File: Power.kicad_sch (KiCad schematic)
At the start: 82 parts, among them J11 8-pin ATX connector, Q1 MMBT2222A, U21 SiRA80DP, U22 TPS25983, U23 AP7361C-33ER, U24 MP8795, U25 MIC23201YML-TR

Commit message: Corrected calculations of MP8795's external components
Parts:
- L2: value 4.7nH -> 4.7uH; footprint Inductor_SMD:L_6.3x6.3_H3 -> Inductor_SMD:L_Coilcraft_XAL1010-XXX; LCSC Part (none) -> C19271849; Mouser Part No  (none) -> 710-7843250072
- L3: value 1.5u -> 1.5uH
- R81: value 8.2k -> 8k; footprint Resistor_SMD:R_0402_1005Metric -> Resistor_SMD:R_0603_1608Metric; LCSC Part C137929 -> C862307
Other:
- note added: "for current ripple 0.00075A"
- note removed: "for current ripple 0.75A"
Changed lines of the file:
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@@
 		)
 	)
-	(text "for current ripple 0.75A"
+	(text "for current ripple 0.00075A"
 		(exclude_from_sim no)
-		(at 134.112 92.456 0)
+		(at 143.51 92.456 0)
 		(effects
 			(font
@@
 			)
 		)
-		(property "Value" "1.5u"
+		(property "Value" "1.5uH"
 			(at 109.22 162.56 90)
 			(effects
@@
 			)
 		)
-		(property "Value" "8.2k"
+		(property "Value" "8k"
 			(at 62.23 120.6499 0)
 			(effects
@@
 			)
 		)
-		(property "Footprint" "Resistor_SMD:R_0402_1005Metric"
+		(property "Footprint" "Resistor_SMD:R_0603_1608Metric"
 			(at 57.912 119.38 90)
 			(effects
@@
 			)
 		)
-		(property "LCSC Part" "C137929"
+		(property "LCSC Part" "C862307"
 			(at 59.69 119.38 0)
 			(effects
@@
 			)
 		)
-		(property "Value" "4.7nH"
+		(property "Value" "4.7uH"
 			(at 118.11 92.202 90)
 			(effects
@@
 			)
 		)
-		(property "Footprint" "Inductor_SMD:L_6.3x6.3_H3"
+		(property "Footprint" "Inductor_SMD:L_Coilcraft_XAL1010-XXX"
 			(at 118.11 93.98 0)
 			(effects
@@
 			(effects
 				(font
+					(size 1.27 1.27)
+				)
+				(hide yes)
+			)
+		)
+		(property "Mouser Part No " "710-7843250072 "
+			(at 118.11 93.98 90)
+			(effects
+				(font
+					(size 1.27 1.27)
+				)
+				(hide yes)
+			)
+		)
+		(property "LCSC Part" "C19271849"
+			(at 118.11 93.98 90)
+			(effects
+				(font

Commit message: minor schematic fixes, footprints changes, layout improvements
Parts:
- C114, C117: footprint Capacitor_THT:C_Radial_D5.0mm_H11.0mm_P2.00mm -> Capacitor_SMD:C_1812_4532Metric; LCSC Part C88755 -> C141660
- L3: LCSC Part (none) -> C520330
- TP7, TP8: footprint TestPoint:TestPoint_Loop_D1.80mm_Drill1.0mm_Beaded -> TestPoint:TestPoint_Pad_D1.0mm
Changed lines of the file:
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@@
 			)
 		)
-		(property "Footprint" "TestPoint:TestPoint_Loop_D1.80mm_Drill1.0mm_Beaded"
+		(property "Footprint" "TestPoint:TestPoint_Pad_D1.0mm"
 			(at 128.27 165.1 0)
 			(effects
@@
 			)
 		)
-		(property "Footprint" "TestPoint:TestPoint_Loop_D1.80mm_Drill1.0mm_Beaded"
+		(property "Footprint" "TestPoint:TestPoint_Pad_D1.0mm"
 			(at 274.32 93.98 0)
 			(effects
@@
 			)
 		)
-		(property "Footprint" "Capacitor_THT:C_Radial_D5.0mm_H11.0mm_P2.00mm"
+		(property "Footprint" "Capacitor_SMD:C_1812_4532Metric"
 			(at 134.3152 172.72 0)
 			(effects
@@
 			)
 		)
-		(property "LCSC Part" "C88755"
+		(property "LCSC Part" "C141660 "
 			(at 133.35 168.91 0)
 			(effects
@@
 			)
 		)
+		(property "LCSC Part" "C520330"
+			(at 109.22 165.1 90)
+			(effects
+				(font
+					(size 1.27 1.27)
+				)
+				(hide yes)
+			)
+		)
 		(pin "1"
 		)
@@
 			)
 		)
-		(property "Footprint" "Capacitor_THT:C_Radial_D5.0mm_H11.0mm_P2.00mm"
+		(property "Footprint" "Capacitor_SMD:C_1812_4532Metric"
 			(at 23.8252 172.72 0)
 			(effects
@@
 			)
 		)
-		(property "LCSC Part" "C88755"
+		(property "LCSC Part" "C141660 "
 			(at 22.86 168.91 0)
 			(effects

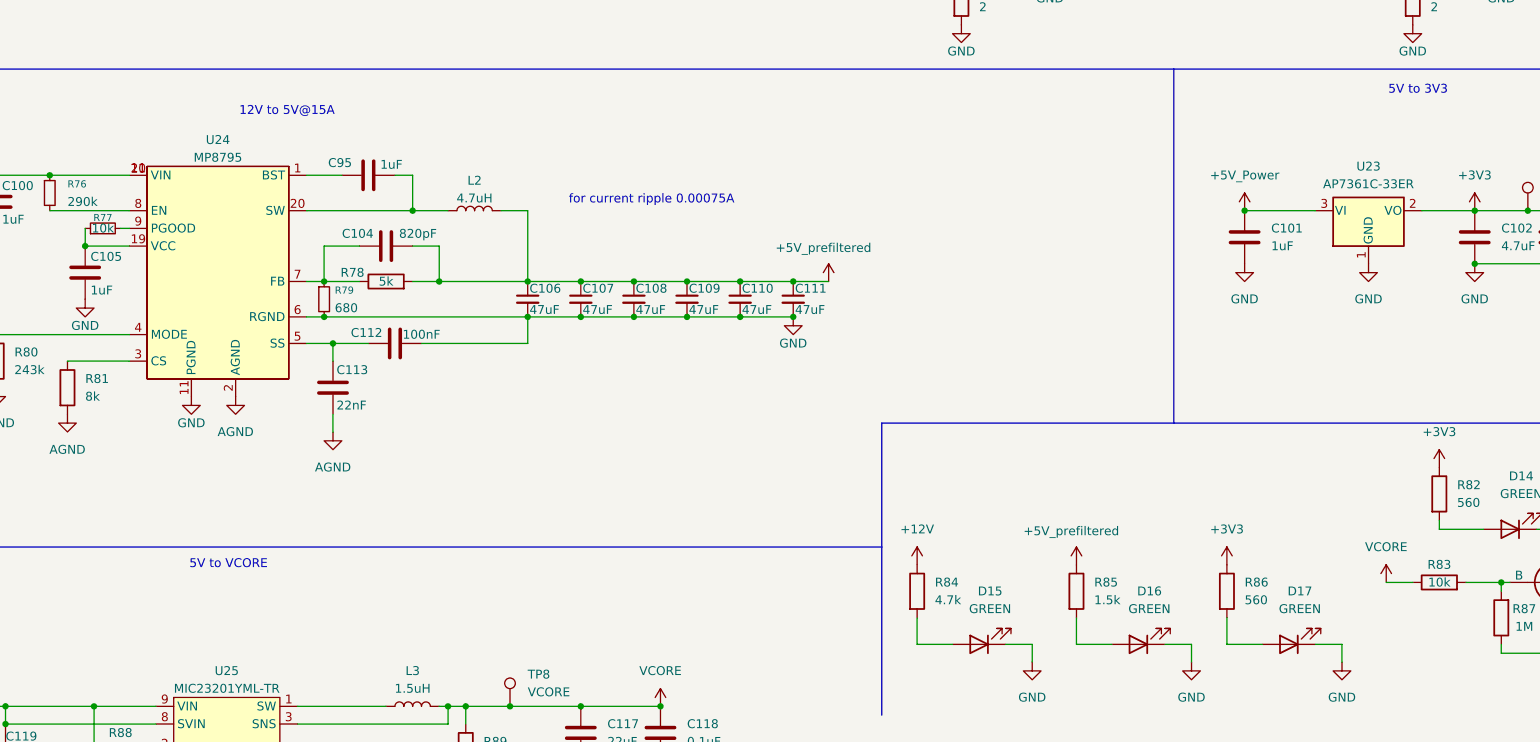
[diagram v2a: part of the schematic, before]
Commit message: comments to schematic added, changed a few components
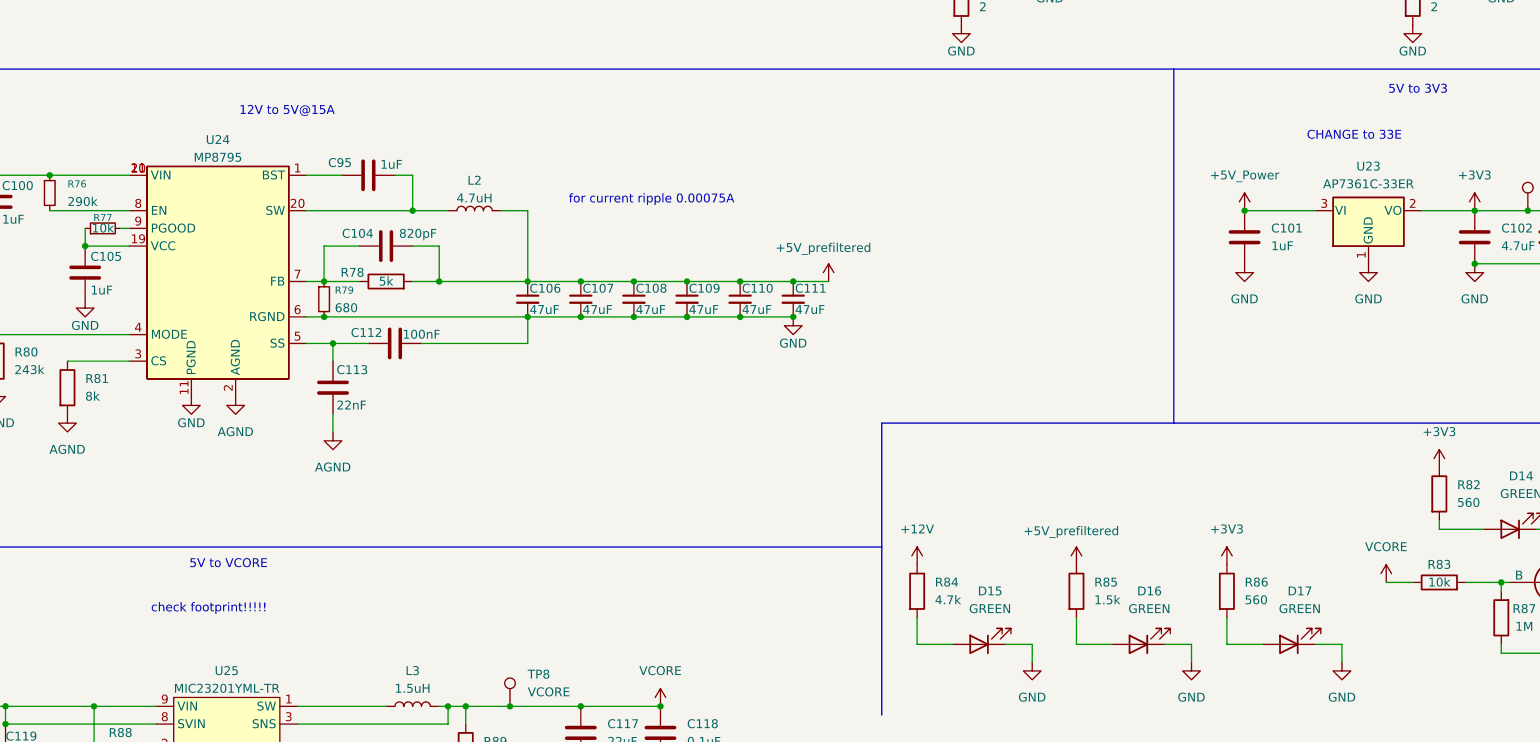
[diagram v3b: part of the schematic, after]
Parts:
- FB1, FB2, FB3: Mouser Part No  (none) -> 710-7427934
- J11: Mouser Part No  (none) -> 538-45586-0005; Mouser Part Number 538-45586-0005 -> (none)
- L2: LCSC Part C19271849 -> C18199458; Mouser Part No  710-7843250072 -> (none)
- U21: Mouser Part No  (none) -> 78-SIRA80DP-T1-RE3
- U22: LCSC Part (none) -> C20611808
- U23: LCSC Part C3743528 -> C500795
- U24: LCSC Part (none) -> C3188708
- U25: Mouser Part No  (none) -> 998-MIC23201YMLTR
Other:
- note added: "CHANGE to 33E"
- note added: "check footprint!!!!!"
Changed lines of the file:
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@@
 		)
 	)
+	(text "check footprint!!!!!"
+		(exclude_from_sim no)
+		(at 80.01 151.13 0)
+		(effects
+			(font
+				(size 1.27 1.27)
+			)
+		)
+	)
+	(text "CHANGE to 33E\n"
+		(exclude_from_sim no)
+		(at 244.348 83.312 0)
+		(effects
+			(font
+				(size 1.27 1.27)
+			)
+		)
+	)
 	(text "for current ripple 0.00075A"
 		(exclude_from_sim no)
@@
 			)
 		)
+		(property "Mouser Part No " "710-7427934 "
+			(at 238.76 52.07 90)
+			(effects
+				(font
+					(size 1.27 1.27)
+				)
+				(hide yes)
+			)
+		)
 		(pin "1"
 		)
@@
 			)
 		)
-		(property "LCSC Part" "C3743528"
+		(property "LCSC Part" "C500795"
 			(at 246.38 93.98 0)
 			(effects
@@
 			)
 		)
+		(property "LCSC Part" "C20611808 "
+			(at 97.79 34.29 0)
+			(effects
+				(font
+					(size 1.27 1.27)
+				)
+				(hide yes)
+			)
+		)
 		(pin "6"
 		)
@@
 			)
 		)
+		(property "Mouser Part No " "710-7427934 "
+			(at 173.99 52.07 90)
+			(effects
+				(font
+					(size 1.27 1.27)
+				)
+				(hide yes)
+			)
+		)
 		(pin "1"
 		)
@@
 			)
 		)
+		(property "Mouser Part No " "998-MIC23201YMLTR "
+			(at 82.55 173.99 0)
+			(effects
+				(font
+					(size 1.27 1.27)
+				)
+				(hide yes)
+			)
+		)
 		(pin "5"
 		)
@@
 			)
 		)
+		(property "Mouser Part No " "78-SIRA80DP-T1-RE3 "
+			(at 134.62 30.48 90)
+			(effects
+				(font
+					(size 1.27 1.27)
+				)
+				(hide yes)
+			)
+		)
 		(pin "3"
 		)
@@
 			)
 		)
-		(property "Mouser Part Number" "538-45586-0005"
+		(property "Mouser Part Number" ""
 			(at 519.05 44.45 0)
 			(effects
@@
 			)
 		)
+		(property "Mouser Part No " "538-45586-0005"
+			(at 24.13 27.94 90)
+			(effects
+				(font
+					(size 1.27 1.27)
+				)
+				(hide yes)
+			)
+		)
 		(pin "1"
 		)
@@
 			)
 		)
-		(property "Mouser Part No " "710-7843250072 "
+		(property "Mouser Part No " ""
 			(at 118.11 93.98 90)
 			(effects
@@
 			)
 		)
-		(property "LCSC Part" "C19271849"
+		(property "LCSC Part" "C18199458"
 			(at 118.11 93.98 90)
 			(effects
@@
 			)
 		)
+		(property "Mouser Part No " "710-7427934 "
+			(at 238.76 25.4 90)
+			(effects
+				(font
+					(size 1.27 1.27)
+				)
+				(hide yes)
+			)
+		)
 		(pin "1"
 		)
@@
 			(at 81.28 102.87 0)
 			(effects
+				(font
+					(size 1.27 1.27)
+				)
+				(hide yes)
+			)
+		)
+		(property "LCSC Part" "C3188708"
+			(at 81.28 102.87 0)
+			(effects

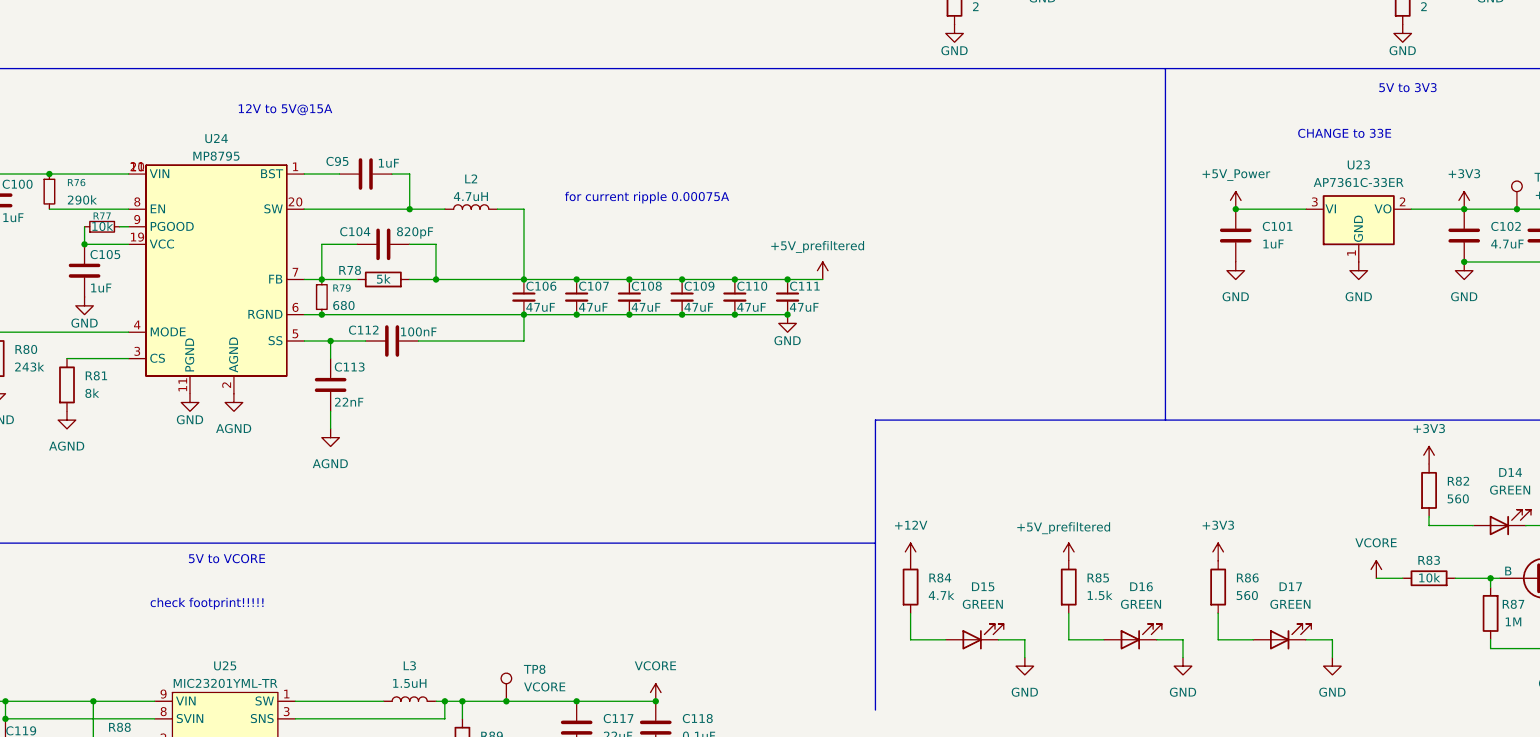
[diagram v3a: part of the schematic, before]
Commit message: AP7361C'sOO footprint changed, Inductors footprint improved
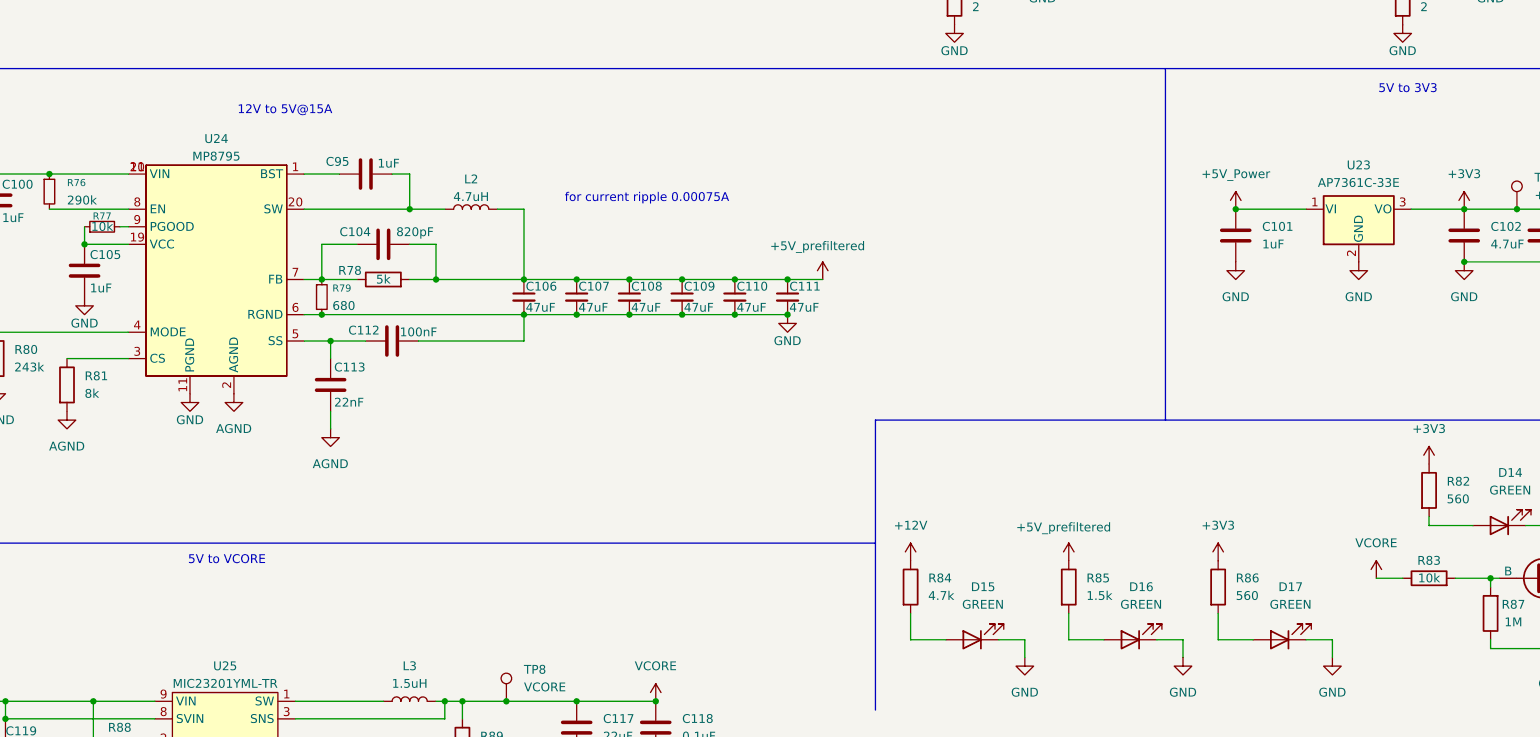
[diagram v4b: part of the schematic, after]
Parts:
- U23: value AP7361C-33ER -> AP7361C-33E
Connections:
- net +3V3: now also U23.3 (VO); no longer U23.2 (VO)
- net +5V_Power: now also U23.1 (VI); no longer U23.3 (VI)
- net GND: now also U23.2 (GND); no longer U23.1 (GND)
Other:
- note removed: "CHANGE to 33E"
- note removed: "check footprint!!!!!"
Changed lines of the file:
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@@
 		)
 	)
-	(text "check footprint!!!!!"
-		(exclude_from_sim no)
-		(at 80.01 151.13 0)
-		(effects
-			(font
-				(size 1.27 1.27)
-			)
-		)
-	)
-	(text "CHANGE to 33E\n"
-		(exclude_from_sim no)
-		(at 244.348 83.312 0)
-		(effects
-			(font
-				(size 1.27 1.27)
-			)
-		)
-	)
 	(text "for current ripple 0.00075A"
 		(exclude_from_sim no)
@@
 			)
 		)
-		(property "Value" "AP7361C-33ER"
+		(property "Value" "AP7361C-33E"
 			(at 246.38 90.17 0)
 			(effects

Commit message: Rearrange of the component placement, scheme changes for better routing
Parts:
- C103, C112, C115, C116, C118, C86, C92, C94: footprint Capacitor_SMD:C_0402_1005Metric -> Capacitor_SMD:C_0201_0603Metric; LCSC Part C5182432 -> C181043
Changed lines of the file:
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@@
 			)
 		)
-		(property "Footprint" "Capacitor_SMD:C_0402_1005Metric"
+		(property "Footprint" "Capacitor_SMD:C_0201_0603Metric"
 			(at 110.49 112.0648 0)
 			(effects
@@
 			)
 		)
-		(property "LCSC Part" "C5182432"
+		(property "LCSC Part" "C181043 "
 			(at 106.68 113.03 90)
 			(effects
@@
 			)
 		)
-		(property "Footprint" "Capacitor_SMD:C_0402_1005Metric"
+		(property "Footprint" "Capacitor_SMD:C_0201_0603Metric"
 			(at 32.7152 172.72 0)
 			(effects
@@
 			)
 		)
-		(property "LCSC Part" "C5182432"
+		(property "LCSC Part" "C181043 "
 			(at 31.75 168.91 0)
 			(effects
@@
 			)
 		)
-		(property "Footprint" "Capacitor_SMD:C_0402_1005Metric"
+		(property "Footprint" "Capacitor_SMD:C_0201_0603Metric"
 			(at 266.3952 59.69 0)
 			(effects
@@
 			)
 		)
-		(property "LCSC Part" "C5182432"
+		(property "LCSC Part" "C181043 "
 			(at 265.43 55.88 0)
 			(effects
@@
 			)
 		)
-		(property "Footprint" "Capacitor_SMD:C_0402_1005Metric"
+		(property "Footprint" "Capacitor_SMD:C_0201_0603Metric"
 			(at 41.6052 172.72 0)
 			(effects
@@
 			)
 		)
-		(property "LCSC Part" "C5182432"
+		(property "LCSC Part" "C181043 "
 			(at 40.64 168.91 0)
 			(effects
@@
 			)
 		)
-		(property "Footprint" "Capacitor_SMD:C_0402_1005Metric"
+		(property "Footprint" "Capacitor_SMD:C_0201_0603Metric"
 			(at 274.0152 101.6 0)
 			(effects
@@
 			)
 		)
-		(property "LCSC Part" "C5182432"
+		(property "LCSC Part" "C181043 "
 			(at 273.05 97.79 0)
 			(effects
@@
 			)
 		)
-		(property "Footprint" "Capacitor_SMD:C_0402_1005Metric"
+		(property "Footprint" "Capacitor_SMD:C_0201_0603Metric"
 			(at 145.7452 172.72 0)
 			(effects
@@
 			)
 		)
-		(property "LCSC Part" "C5182432"
+		(property "LCSC Part" "C181043 "
 			(at 144.78 168.91 0)
 			(effects
@@
 			)
 		)
-		(property "Footprint" "Capacitor_SMD:C_0402_1005Metric"
+		(property "Footprint" "Capacitor_SMD:C_0201_0603Metric"
 			(at 266.3952 33.02 0)
 			(effects
@@
 			)
 		)
-		(property "LCSC Part" "C5182432"
+		(property "LCSC Part" "C181043 "
 			(at 265.43 29.21 0)
 			(effects
@@
 			)
 		)
-		(property "Footprint" "Capacitor_SMD:C_0402_1005Metric"
+		(property "Footprint" "Capacitor_SMD:C_0201_0603Metric"
 			(at 201.6252 59.69 0)
 			(effects
@@
 			)
 		)
-		(property "LCSC Part" "C5182432"
+		(property "LCSC Part" "C181043 "
 			(at 200.66 55.88 0)
 			(effects
